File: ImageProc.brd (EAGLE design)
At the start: 49.8 x 23.2 mm, 114 parts, among them IC1 XC61GC3002HR-G, IC10 AT45DB642D-CNU, IC2 MIC5335-SPYMT, IC3 MIC5335-JGYMT, IC5 AT86RF233-ZU, IC6 LTC6088, IC7 DRV8833RTY, IC8 DRV8833RTY, IC9 MPU-6000, P1 BAT+, P10 MD2, P11 EXT1, P12 EXT2, P13 EXT3, P14 EXT4, P16 EXT5, P2 BAT-, P3 MA1, P4 MA2, P5 MB1, P6 MB2, P7 MC1, P8 MC2, P9 MD1, U1 CY8C5688LTI-LP086

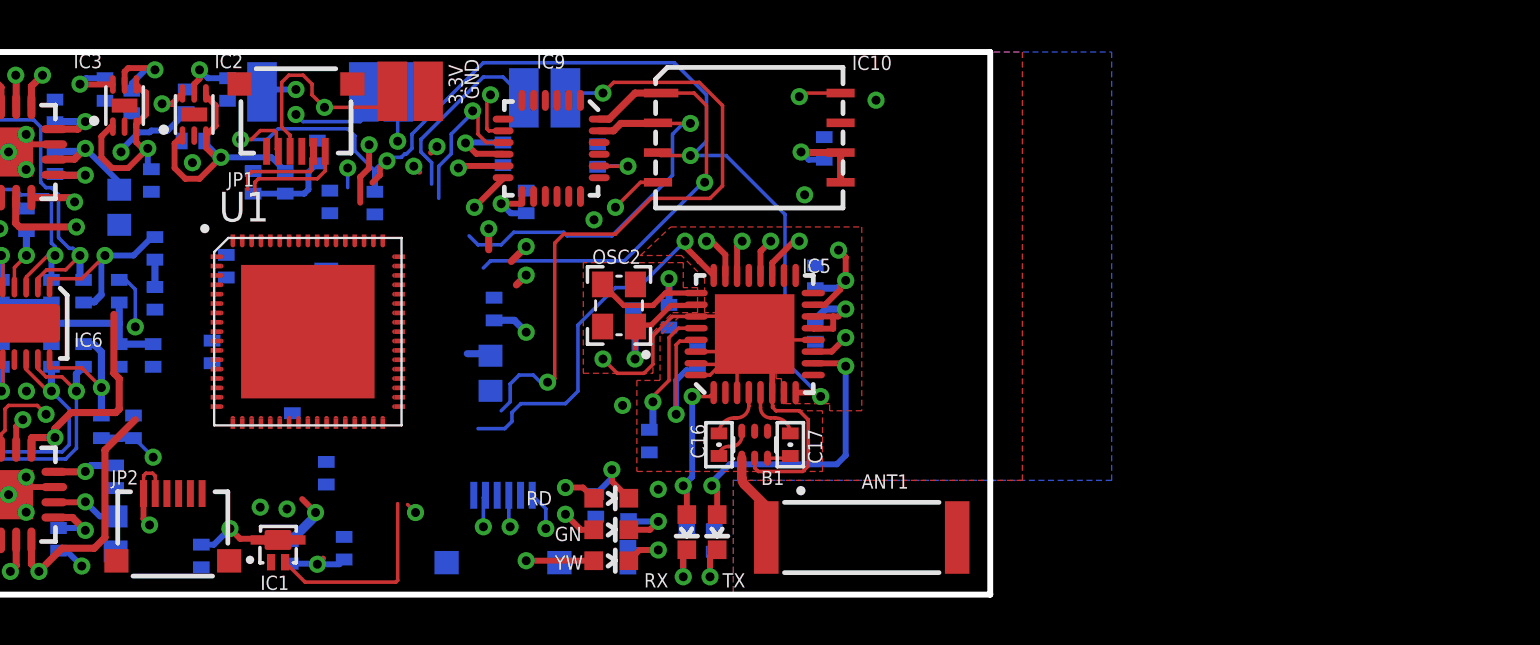
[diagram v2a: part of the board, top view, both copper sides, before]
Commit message: Removed flash, ripping up more routing, added SD card
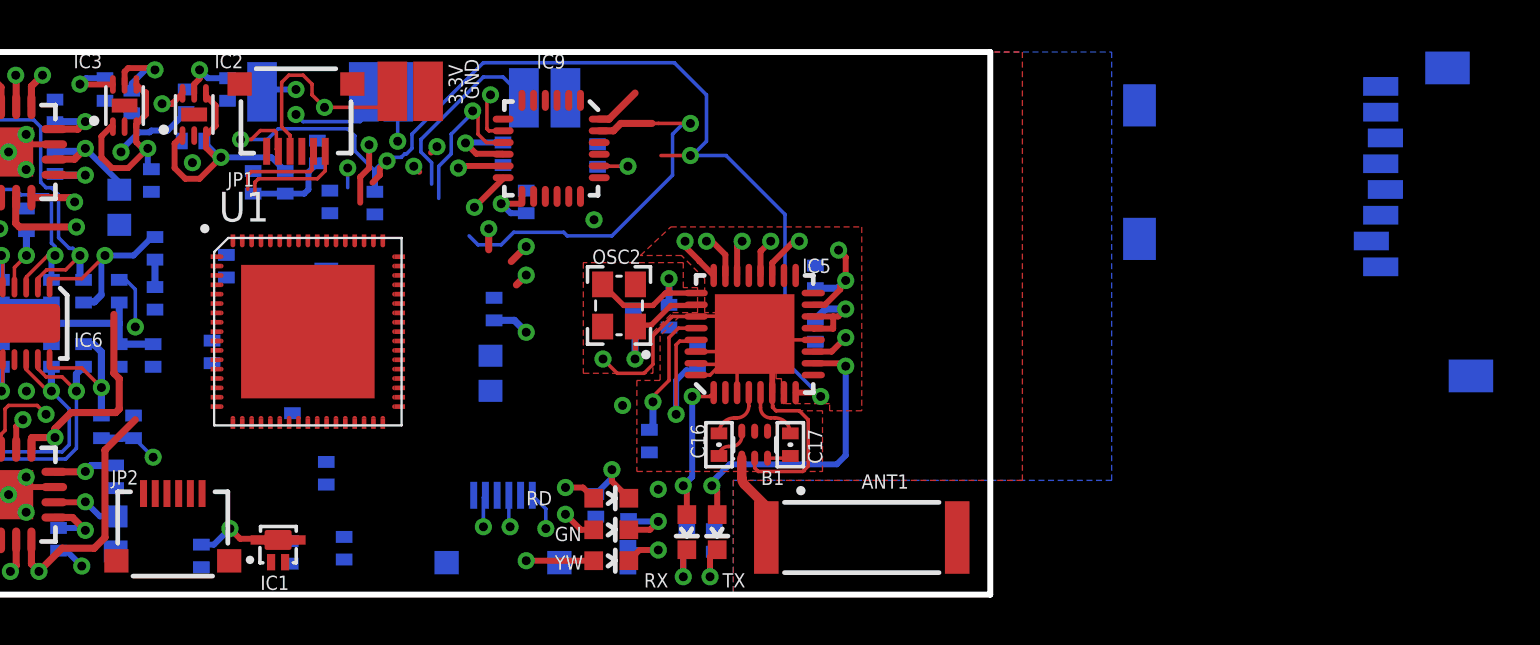
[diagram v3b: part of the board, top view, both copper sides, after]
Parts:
- removed C40: 0.1uF, biomimetic:0402-CAP
- removed IC10: AT45DB642D-CNU, biomimetic:CASON-8
- added U2: USD-SOCKETNEW, SparkFun-Connectors:MICRO-SD-SOCKET-PP
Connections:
- removed net !SS2_1: IC10.4
- net !RESET: no longer IC10.3
- net 3.3V: no longer C40.1, IC10.5, IC10.6
- net GND: no longer C40.2, IC10.7
- net SCK2: no longer IC10.2
- net SDI2: no longer IC10.8
- net SDO2: no longer IC10.1
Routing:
- net IC3/INT3/RD10: track 28.5 -> 0.00 mm, vias 2 -> 0
- net SDO2: track 19.7 -> 1.99 mm, vias 1 -> 0
- net RADIO_IRQ: track 16.5 -> 1.97 mm, vias 2 -> 1
- net LOWBATT_IRQ: track 8.47 -> 0.00 mm
- net 3.3V: track 40.8 -> 34.0 mm, vias 13 -> 11
- net V_BATT: track 44.5 -> 41.0 mm, vias 10 -> 9
- net SDA1: track 3.86 -> 1.38 mm, vias 2 -> 1
- net !SS2_1: track 4.89 -> 2.63 mm, vias 2 -> 1
- net SDI2: track 8.79 -> 6.72 mm, vias 2 -> 1
- net N$28: track 1.03 -> 0.35 mm
- net SDI1: track 1.87 -> 1.64 mm, vias 2 -> 1
- net SCK1: track 2.28 -> 2.07 mm, vias 2 -> 1
- net GND: vias 20 -> 18

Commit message: Still removing small elemets from existing IP2.5
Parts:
- moved U2 21.8 mm to (34.0, 22.6)
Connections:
- removed net !RESET: IC5.8, JP1.5, R3.1
- removed net PGC: JP1.1
- removed net PGD: JP1.2
- new net !XRES: IC5.8, JP1.3, R3.1
- new net SWD_SCLK: JP1.4
- new net SWD_SDAT: JP1.5
- net 3.3V: now also JP1.1; no longer JP1.4
- net GND: now also JP1.2; no longer JP1.3
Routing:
- net !RESET: track 47.5 -> 0.00 mm, vias 4 -> 0
- net SCK2: track 16.9 -> 0.00 mm, vias 1 -> 0
- net !XRES: track 0.00 -> 14.8 mm, vias 0 -> 3
- net 3.3V: track 34.0 -> 23.6 mm, vias 11 -> 9
- net AN5/QEB/IC8/RB5: track 7.96 -> 0.00 mm
- net SDI2: track 6.72 -> 0.08 mm, vias 1 -> 0
- net PGC: track 4.57 -> 0.00 mm
- net PGD: track 4.26 -> 0.00 mm
- net N$29: track 2.55 -> 0.00 mm, vias 1 -> 0
- net SDO2: track 1.99 -> 0.00 mm
- net MOTOR_B_IN1: track 4.66 -> 3.76 mm, vias 2 -> 1
- net MOTOR_C_IN2: track 9.99 -> 9.09 mm, vias 2 -> 1
- net MOTOR_A_IN1: track 1.92 -> 1.33 mm, vias 3 -> 2
- net GND: vias 18 -> 16

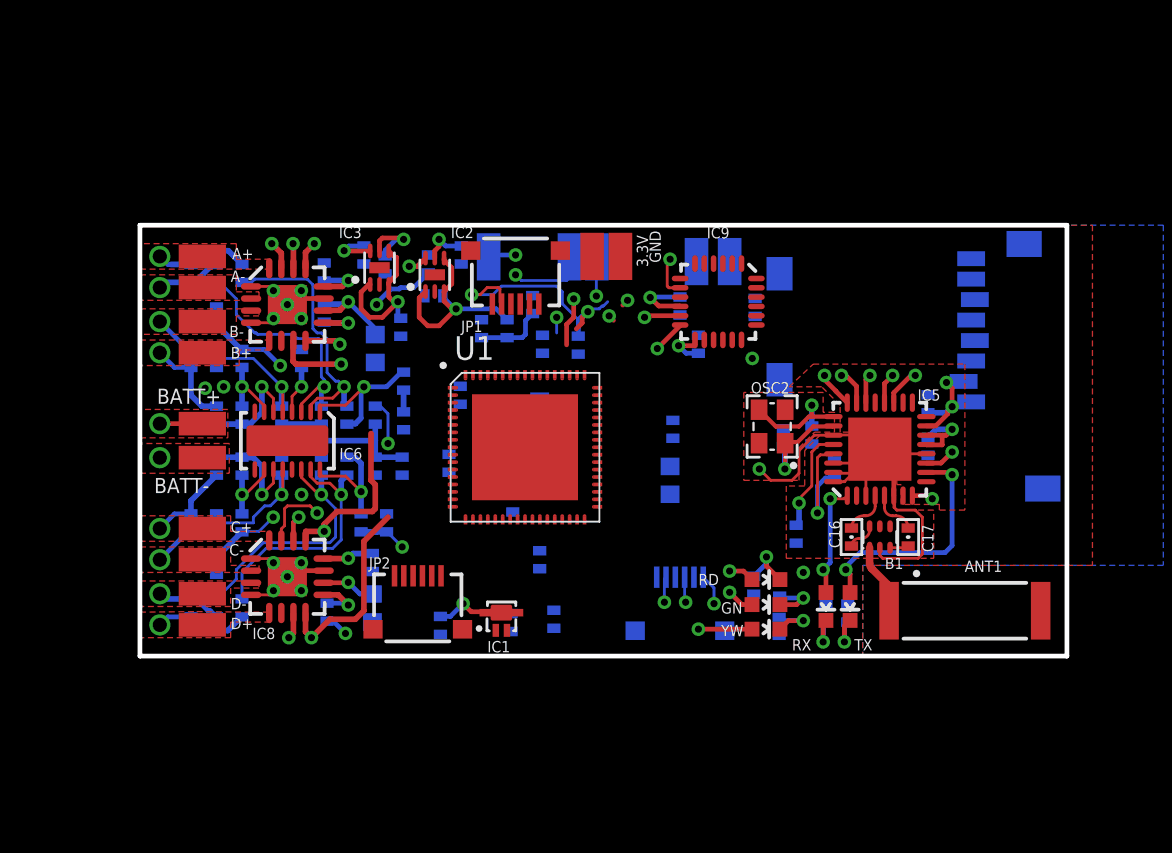
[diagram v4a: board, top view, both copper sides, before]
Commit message: Changed to resistor arrays. SD card footprint updated. Much routing removed.
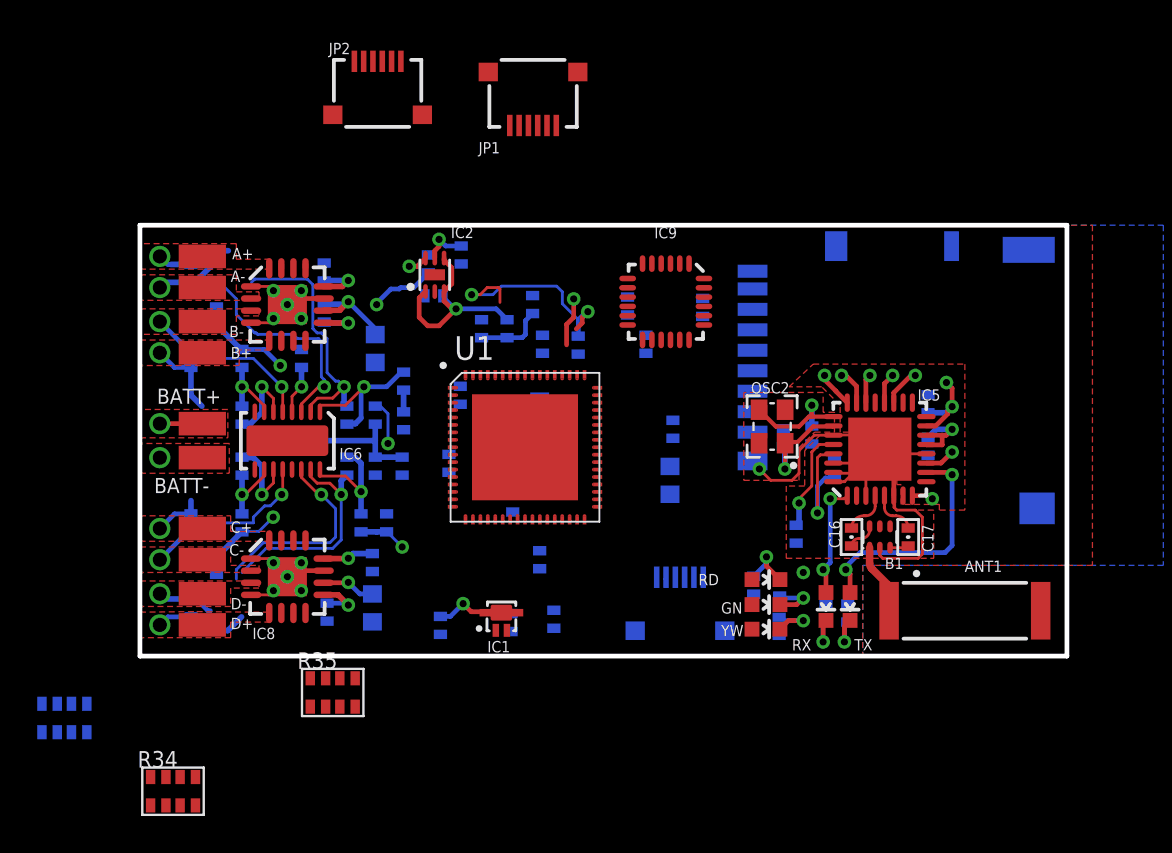
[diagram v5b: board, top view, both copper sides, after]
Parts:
- removed 3.3V, GND, P16: EXT5, wirepad:SMD1,27-2,54
- removed C2, C5, C8: 1uF, biomimetic:0402-CAP
- removed IC3: MIC5335-JGYMT, biomimetic:MLF-6
- removed P11: EXT1, wirepad:SMD1,27-2,54
- removed P12: EXT2, wirepad:SMD1,27-2,54
- removed P13: EXT3, wirepad:SMD1,27-2,54
- removed P14: EXT4, wirepad:SMD1,27-2,54
- removed R10, R13, R14, R19, R20, R23, R24, R9: 47k, biomimetic:0402-RES
- removed R11, R15, R21, R25: 15k, biomimetic:0402-RES
- removed U2: USD-SOCKETNEW, SparkFun-Connectors:MICRO-SD-SOCKET-PP
- added J1: CON-HRS-DM3AT, pullin:HRS-DM3AT
- added R33, R34: 47k, OPL Eagle Library:R1206-8
- added R35: 15k, OPL Eagle Library:R1206-8
- moved JP2 27.7 mm to (12.8, 30.3)
- moved JP1 9.65 mm to (21.1, 30.3)
- moved C37 2.82 mm to (27.2, 16.8)
- moved IC9 2.82 mm to (28.3, 19.1)
- moved C38 2.82 mm to (30.3, 18.7)
- moved C39 2.82 mm to (26.2, 18.8)
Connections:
- removed net 1.8V: C8.1, IC3.5
- removed net 2.5V: C2.1, IC3.6
- removed net AN1/RB1: P11.1
- removed net AN3/INDX/RB3: P12.1
- removed net AN4/QEA/IC7/RB4: P13.1
- removed net AN5/QEB/IC8/RB5: P14.1
- removed net IC3/INT3/RD10: P16.1
- new net VDD: J1.4
- new net VSS: J1.6
- net 3.3V: no longer 3.3V.1
- net GND: no longer C2.2, C5.1, C8.2, GND.1, IC3.2, IC3.EPAD
- net MOTOR_A_OUT1: no longer R9.1
- net MOTOR_A_OUT2: no longer R10.1
- net MOTOR_B_OUT1: no longer R13.1
- net MOTOR_B_OUT2: no longer R14.1
- net MOTOR_C_OUT1: no longer R19.1
- net MOTOR_C_OUT2: no longer R20.1
- net MOTOR_D_OUT1: no longer R23.1
- net MOTOR_D_OUT2: no longer R24.1
- net N$22: now also R33.6; no longer R13.2
- net N$23: now also R33.5, R35.2; no longer R14.2, R15.2
- net N$24: now also R34.8; no longer R19.2
- net N$25: now also R34.7, R35.3; no longer R20.2, R21.2
- net N$26: now also R34.6; no longer R23.2
- net N$27: now also R34.5, R35.4; no longer R24.2, R25.2
- net N$30: now also R33.8; no longer R9.2
- net N$31: now also R33.7, R35.1; no longer R10.2, R11.2
- net V_BATT: no longer C5.2, IC3.1, IC3.3, IC3.4
- net V_REF: no longer R11.1, R15.1, R21.1, R25.1
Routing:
- net V_BATT: track 41.0 -> 25.9 mm, vias 9 -> 5
- net MOTOR_D_IN2: track 10.9 -> 0.00 mm, vias 2 -> 0
- net MOTOR_C_IN2: track 9.09 -> 0.00 mm, vias 1 -> 0
- net V_REF: track 11.8 -> 6.12 mm
- net 3.3V: track 23.6 -> 18.0 mm, vias 9 -> 6
- net AN3/INDX/RB3: track 4.35 -> 0.00 mm, vias 1 -> 0
- net MOTOR_B_IN1: track 3.76 -> 0.00 mm, vias 1 -> 0
- net 1.8V: track 3.48 -> 0.00 mm, vias 1 -> 0
- net N$32: track 3.42 -> 0.00 mm, vias 1 -> 0
- net YW_LED: track 2.88 -> 0.00 mm, vias 1 -> 0
- net 2.5V: track 2.59 -> 0.00 mm, vias 1 -> 0
- net N$27: track 13.6 -> 11.1 mm
- net AN4/QEA/IC7/RB4: track 2.37 -> 0.00 mm, vias 1 -> 0
- net !SS2_2: track 2.62 -> 0.38 mm, vias 1 -> 0
- net CAM_HREF: track 1.95 -> 0.00 mm, vias 1 -> 0
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
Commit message: Major board layout jumble. Lots of placeholder connections.
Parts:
- removed R12, R17, R22: 15k, biomimetic:0402-RES
- removed R16, R18: 4.7k, biomimetic:0402-RES
- added JP6: USBSMD, SparkFun-Connectors:USB-MINIB
- R8: device biomimetic:0402-RES -> OPL Eagle Library:R1206-8
- moved R33 35.3 mm to (5.13, 30.7)
- moved R26 20.6 mm to (29.2, 21.6)
- moved LED1 20.3 mm to (30.5, 21.5), turned to 0 degrees
- moved LED2 18.8 mm to (31.8, 21.5), turned to 0 degrees
- moved R35 18.7 mm to (-2.92, 11.2), flipped to the bottom
- moved R27 18.2 mm to (30.5, 21.5), turned to 270 degrees
- moved R28 17.8 mm to (31.8, 21.5)
- moved C23 17.4 mm to (25.9, 8.03), turned to 0 degrees
- moved LED3 17.4 mm to (33.2, 21.5), turned to 0 degrees
- moved C14 17.2 mm to (32.4, -4.56)
- moved R34 15.7 mm to (-3.04, 7.66), flipped to the bottom, turned to 180 degrees
- moved JP2 15.4 mm to (25.1, 21.0), turned to 180 degrees
- moved C22 14.6 mm to (28.1, 8.03), turned to 0 degrees
- moved OSC2 14.5 mm to (27.1, -0.36), turned to 180 degrees
- moved C18 13.4 mm to (27.7, 0.25), turned to 0 degrees
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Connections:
- removed net !SS2_2: IC9.8
- removed net VDD: J1.4
- removed net VSS: J1.6
- new net !SS2: IC9.8, U1.39
- new net EMFILE_CS: U1.14
- new net EMFILE_MISO: U1.15
- new net EMFILE_MOSI: U1.16
- new net EMFILE_SCK: U1.18
- new net USB_D+: JP6.D+, U1.55
- new net USB_D-: JP6.D-, U1.56
- net !SS1: now also U1.37
- net 3.3V: now also J1.4; no longer R16.2
- net BATT_LEVEL: now also U1.11
- net GND: now also J1.6; no longer R18.1
- net GN_LED: now also U1.19
- net MOTOR_A_BEMF: now also U1.1
- net MOTOR_A_IN1: now also U1.28
- net MOTOR_A_IN2: now also U1.29
- net MOTOR_B_BEMF: now also U1.2
- net MOTOR_B_IN1: now also U1.30
- net MOTOR_B_IN2: now also U1.31
- net MOTOR_C_BEMF: now also U1.3
- net MOTOR_C_IN1: now also U1.32
- net MOTOR_C_IN2: now also U1.33
- net MOTOR_D_BEMF: now also U1.4
- net MOTOR_D_IN1: now also U1.34
- net MOTOR_D_IN2: now also U1.36
- net N$22: now also R8.2; no longer R12.1
- net N$24: now also R8.3; no longer R17.1
- net N$26: now also R8.4; no longer R22.1
- net N$34: now also R8.5; no longer R22.2
- net N$35: now also R8.6; no longer R17.2
- net N$36: now also R8.8; no longer R8.2
- net N$37: now also R8.7; no longer R12.2
- net RD_LED: now also U1.23
- net SCK1: now also U1.48
- net SCK2: now also U1.49
- net SCL1: now also U1.50
- net SDA1: now also U1.51
- net SDI1: now also U1.40
- net SDI2: now also U1.41
- net SDO1: now also U1.46
- net SDO2: now also U1.47
- net V_REF: no longer R16.1, R18.2
- net YW_LED: now also U1.27
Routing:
- net !XRES: track 13.5 -> 1.14 mm, vias 3 -> 1
- net N$30: track 13.6 -> 2.58 mm, vias 1 -> 0
- net N$31: track 12.0 -> 2.03 mm, vias 1 -> 0
- net N$26: track 12.1 -> 2.43 mm, vias 1 -> 0
- net N$27: track 11.1 -> 2.37 mm
- net V_REF: track 6.12 -> 0.00 mm
- net N$25: track 5.75 -> 1.37 mm, vias 1 -> 0
- net N$23: track 5.57 -> 1.37 mm, vias 1 -> 0
- net N$17: track 2.84 -> 0.00 mm, vias 1 -> 0
- net N$15: track 2.82 -> 0.00 mm, vias 1 -> 0
- net N$16: track 2.72 -> 0.00 mm, vias 1 -> 0
- net N$22: track 4.30 -> 1.60 mm, vias 1 -> 0
- net !SS2_1: track 2.63 -> 0.00 mm, vias 1 -> 0
- net 3.3V: track 18.0 -> 15.5 mm, vias 6 -> 5
- net N$24: track 4.39 -> 1.96 mm
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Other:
- board size 49.8 x 23.2 mm -> 44 x 23.2 mm
